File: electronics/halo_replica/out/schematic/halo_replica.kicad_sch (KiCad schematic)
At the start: 57 parts, among them J1 U.FL / IPEX MHF RECEPTACLE, U1 nRF52832-CIAA (WLCSP-50) - DR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, U2 APPLE U1 UWB SiP - DNP / UNPO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, U3 GD25LQ32C 32Mb 1.8V SPI NOR (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, U4 3-AXIS ACCELEROMETER - PART C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, U5 MAX98357A-CLASS CLASS-D AMP (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, U6 TPS62746-CLASS BUCK 3V->1V8 (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, U7 TLV9001-CLASS OP-AMP - ROLE I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, U8 FPF2487-CLASS LOAD SWITCH (LO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, U9 CANNOT DETERMINE - marking 1A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, X1 32 MHz? marking T320 / RBEV -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, X2 32.768 kHz? marking A048L - P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

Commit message: E07 synthesis: three kinds of adjacent, and the pipeline exit code as a sixth
Refinement from the comparison lane: the five cases differ in WHAT the adjacent
property was - three adjacent STATISTICS (increment permutation, off-peak noise,
area alone), one adjacent COORDINATE (between-in-x), one adjacent PATH (a guard
resolving against the search root). The path case is the one people least expect
because it is not a modelling error at all - a plumbing error wearing a control's
clothes, which no amount of thinking about the physics would have found.

Plus a sixth of the same shape from the same day: reading 'cmd | tail's exit
status instead of the command's. PIPESTATUS[0] gives the real one. The exit code
you read was adjacent to the exit code you wanted.

Co-Authored-By: Claude Opus 5 (1M context) <noreply@anthropic.com>
Claude-Session: https://claude.ai/code/session_01JRY3feHovaK2VS3mL7infx
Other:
- note added: "halo REPLICA - Apple AirTag A2187 (FCC ID BCGA2187), reconstructed. NOBODY HAS TRACED APPLE'S COPPER. Not one net here was read off a board. Every net carries a basis - MEASURED, INFERRED or CHOSEN - and NETS.md beside this file lists all of them. ONLY SEVEN OF 51 NETS ARE MEASURED: the three battery contacts and the four SWD pads O'Flynn published. The other 44 are 21 INFERRED and 23 CHOSEN."
- note removed: "halo REPLICA - Apple AirTag A2187 (FCC ID BCGA2187), reconstructed. NOBODY HAS TRACED APPLE'S COPPER. Not one net here was read off a board. Every net carries a basis - MEASURED, INFERRED or CHOSEN - and NETS.md beside this file lists all of them. Only five nets are MEASURED, and they are the SWD pads."
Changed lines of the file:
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@@
 		)
 	)
-	(text "halo REPLICA - Apple AirTag A2187 (FCC ID BCGA2187), reconstructed. NOBODY HAS TRACED APPLE'S COPPER. Not one net here was read off a board. Every net carries a basis - MEASURED, INFERRED or CHOSEN - and NETS.md beside this file lists all of them. Only five nets are MEASURED, and they are the SWD pads."
+	(text "halo REPLICA - Apple AirTag A2187 (FCC ID BCGA2187), reconstructed. NOBODY HAS TRACED APPLE'S COPPER. Not one net here was read off a board. Every net carries a basis - MEASURED, INFERRED or CHOSEN - and NETS.md beside this file lists all of them. ONLY SEVEN OF 51 NETS ARE MEASURED: the three battery contacts and the four SWD pads O'Flynn published. The other 44 are 21 INFERRED and 23 CHOSEN."
 		(exclude_from_sim no)
 		(at 12.7 388.62 0)

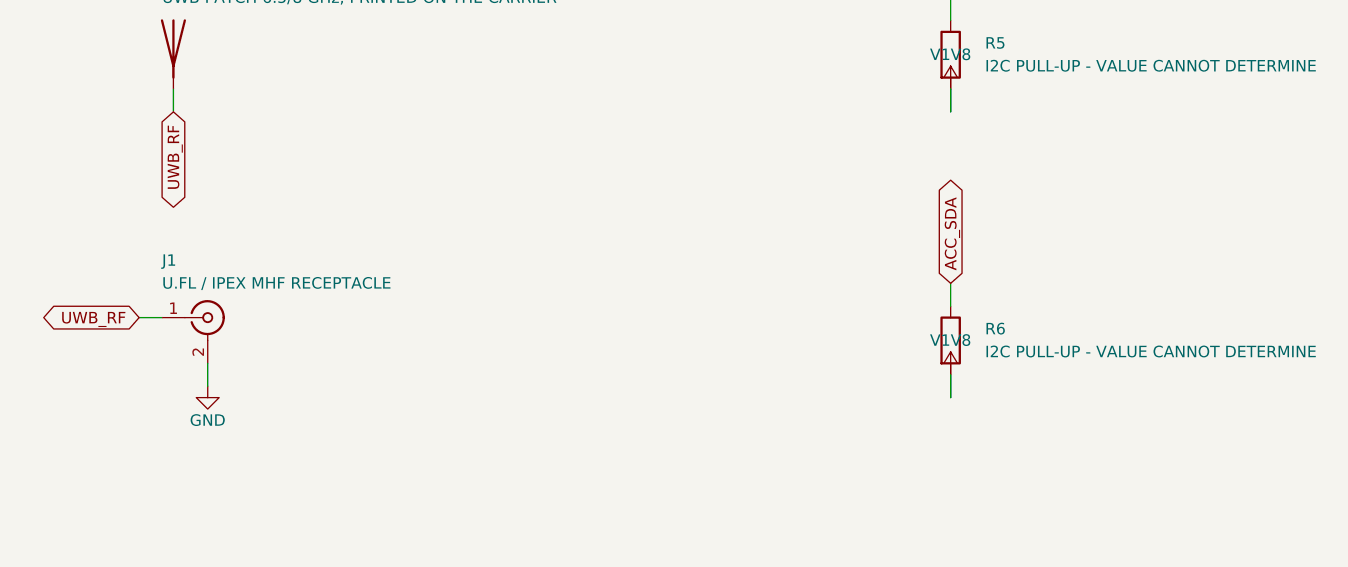
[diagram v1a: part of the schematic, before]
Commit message: L9: three legs - EXISTS, CURRENT, VALID. Existence is adjacent to currency, currency to validity
halo-cb refused to give us a clean test case and that refusal produced the third leg. It
is deliberately NOT regenerating rev_a's gerbers because the board still has 28
unconnected nets: a set cut now would be FRESH AND UNBUILDABLE, and would pass existence
AND freshness simultaneously. That is a worse artifact than a stale one precisely because
both other assertions wave it through.

  EXISTS   a file of the right kind is here and the tool can open it
  CURRENT  it is newer than every one of its sources
  VALID    its source PASSED ITS OWN CHECKS at the time it was cut

Not belt-and-braces: three genuinely different properties one artifact can independently
fail, each satisfied by something NEXT TO what we actually want.

RUN AGAINST BOTH BOARDS. rev_a: 8 of 8 exist and open - I WAS WRONG THAT IT HAD NO
GERBERS, there are twelve plus two drill files, just under out/release/board/gerber where
I had not searched. The conclusion survives for two worse reasons:
  D6 DRC     STALE by 17,616 s - it grades copper it never saw
  D7 gerbers STALE by 7,742 s AND INVALID - cut from a board with 28 unconnected nets
  D8 drill   STALE by 7,741 s AND INVALID - same
Replica: 5 of 8 exist, D2 netlist was 81 s older than its schematic when first run.

FOUR DEFECTS IN MY OWN CHECK, each found by pointing it somewhere new:
 1. The D7 glob was **/*.gbr, which catches only the DRILL MAPS. A real KiCad gerber set
    is .gtl .gbl .g1 .g2 .gts .gbs .gto .gbo .gm1 - none end in .gbr. It would have called
    a set complete while seeing none of its copper layers.
 2. The DRC probe was the bare substring "drc", which admitted drc-liveness.json and
    friends - not DRC reports at all. Now the KiCad $schema URL.
 3. read_verdict SUMMED every matching report, adding up several runs against several
    different boards and returning 1016 errors that belonged to none of them. A verdict is
    a prop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
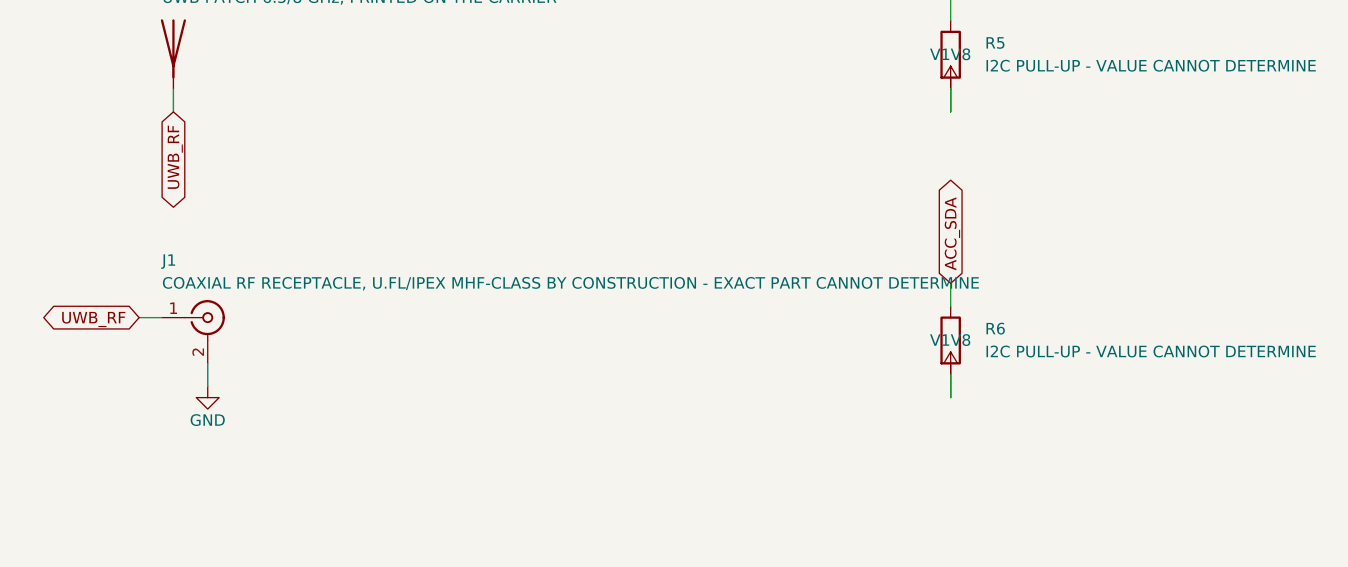
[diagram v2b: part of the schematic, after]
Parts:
- J1: value U.FL / IPEX MHF RECEPTACLE -> COAXIAL RF RECEPTACLE, U.FL/IPEX MHF-CLASS BY CONSTRUCTION - EXACT PART CANNOT DETERMINE
- X1: BOM confidence HIGH that the marking is T320 / RBEV. CANNOT DETERMINE for the manufacturer, the part number, the load capacitance and the tolerance. MEDIUM for 'this is the 32 MHz one' — that is -> HIGH that the marking is T320 / RBEV. CANNOT DETERMINE for the manufacturer, the part number, the load capacitance and the tolerance. MEDIUM for 'this is the 32 MHz one' — Catley's
- X2: BOM confidence HIGH for the marking. CANNOT DETERMINE for the part. MEDIUM for the frequency assignment, untested. -> HIGH for the marking. CANNOT DETERMINE for the part. MEDIUM for the frequency assignment, now TESTED by package geometry and SUPPORTED (see X1_vs_X2_TEST). Its aspect 1.554 and 161
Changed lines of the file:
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@@
 			)
 		)
-		(property "BOM confidence" "HIGH that the marking is T320 / RBEV. CANNOT DETERMINE for the manufacturer, the part number, the load capacitance and the tolerance. MEDIUM for 'this is the 32 MHz one' — that is "
+		(property "BOM confidence" "HIGH that the marking is T320 / RBEV. CANNOT DETERMINE for the manufacturer, the part number, the load capacitance and the tolerance. MEDIUM for 'this is the 32 MHz one' — Catley's"
 			(at 300.99 36.83 0)
 			(effects
@@
 			)
 		)
-		(property "BOM confidence" "HIGH for the marking. CANNOT DETERMINE for the part. MEDIUM for the frequency assignment, untested."
+		(property "BOM confidence" "HIGH for the marking. CANNOT DETERMINE for the part. MEDIUM for the frequency assignment, now TESTED by package geometry and SUPPORTED (see X1_vs_X2_TEST). Its aspect 1.554 and 161"
 			(at 300.99 64.77 0)
 			(effects
@@
 			)
 		)
-		(property "Value" "U.FL / IPEX MHF RECEPTACLE"
+		(property "Value" "COAXIAL RF RECEPTACLE, U.FL/IPEX MHF-CLASS BY CONSTRUCTION - EXACT PART CANNOT DETERMINE"
 			(at 441.96 96.52 0)
 			(effects

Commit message: L9: the fifth state - whose fault a clearance violation is, with the guard that stops it being a string
Three classes, and the excusing ones must PROVE it:
  DRAWN-WRONG          no pointer, BLOCKS. Our defect, and THE DEFAULT.
  MEASUREMENT-LIMITED  pointer required, BLOCKS. Not our defect and still not fabricable
                       - you cannot cut a board where two pads overlap whatever the
                       reason. It names a different fix: a measurement that can separate
                       them, not a nudged pad.
  GENUINELY-TOUCHING   pointer required, does NOT block. Same net or same feature, so
                       there is no clearance to violate.

THE DEFAULT IS THE WHOLE INCENTIVE. An unclassified violation falls back to DRAWN-WRONG,
so SILENCE MEANS OUR FAULT, NEVER APPLE'S. A lane that wants a violation excused must
produce evidence; a lane that produces nothing gets the blame.

AND THE GUARD IS THE POINT, because I raised this failure mode against the basis counter
an hour ago and it applies to my own gate: IF A VIOLATION CAN LEAVE DRAWN-WRONG BY
EDITING A STRING, THE GATE IS SOMETHING A LANE IMPROVES BY TYPING. So an excusing class
names evidence this check RESOLVES and then checks that it SUPPORTS THE CLAIM.

6 breaks, and C-4 is the one that matters:
  C-1  no classification file            -> all DRAWN-WRONG
  C-2  gap 0.0500 mm, pointer resolves   -> MEASUREMENT-LIMITED accepted
  C-3  same claim, pointer does not resolve        -> refused
  C-3b pointer resolves, names a row NOT in it     -> refused
  C-4  POINTER RESOLVES, gap 0.0900 mm is OUTSIDE the 0.0606 floor -> REFUSED
  C-5  GENUINELY-TOUCHING accepted and does not block
RESOLVING IS NOT SUPPORTING. Without C-4 the excuse is a string with a filename attached.

THE FLOOR IS DERIVED AND SAYS SO: 0.0606 mm = two genuine pixels at 33 px/mm, one edge-
location pixel on each of the two facing edges. NOT the registration hold-out of
0.1256 mm, which would excuse roughly twice as m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
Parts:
- added TP19: SPI_MOSI (O'Flynn TP19), TestPoint:TestPoint_Pad_D1.0mm, symbol Connector:TestPoint
- added TP20: SPI_MISO (O'Flynn TP20), TestPoint:TestPoint_Pad_D1.0mm, symbol Connector:TestPoint
- added TP21: V1V8_SW (O'Flynn TP21), TestPoint:TestPoint_Pad_D1.0mm, symbol Connector:TestPoint
- added TP22: SPI_SCK (O'Flynn TP22), TestPoint:TestPoint_Pad_D1.0mm, symbol Connector:TestPoint
- added TP24: FLASH_nCS (O'Flynn TP24), TestPoint:TestPoint_Pad_D1.0mm, symbol Connector:TestPoint
- added TP29: GND (O'Flynn TP29), TestPoint:TestPoint_Pad_D1.0mm, symbol Connector:TestPoint
- added TP34: V1V8 (O'Flynn TP34), TestPoint:TestPoint_Pad_D1.0mm, symbol Connector:TestPoint
- added TP5: VBAT_SNS_P2 (O'Flynn TP5), TestPoint:TestPoint_Pad_D1.0mm, symbol Connector:TestPoint
- added TP6: VBAT_RAW (O'Flynn TP6), TestPoint:TestPoint_Pad_D1.0mm, symbol Connector:TestPoint
- added TP7: GND (O'Flynn TP7), TestPoint:TestPoint_Pad_D1.0mm, symbol Connector:TestPoint
- added TP9: P0.26 - FUNCTION CANNOT DETERMINE, TestPoint:TestPoint_Pad_D1.0mm, symbol Connector:TestPoint
- TP30: Note O'Flynn's TP30 = nRST. On nRF52832 that is P0.21/nRESET. TH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 -> O'Flynn's table, verbatim: '30 | nRF ball H1 (P0.21/nRST)'.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; Source research/fetched/A-oflynn-testpoints-and-glitch-repos.md -> research/fetched/A-oflynn-testpoints-and-glitch-repos.md — 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
- TP31: Note O'Flynn's TP31 = SWO, P0.18 on this die. THESE FOUR ARE THE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 -> O'Flynn's table, verbatim: '31 | nRF ball H2 (P0.18/SWO)'. 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; Source research/fetched/A-oflynn-testpoints-and-glitch-repos.md -> research/fetched/A-oflynn-testpoints-and-glitch-repos.md — 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
- TP35: Note O'Flynn's TP35 = SWCLK. THESE FOUR ARE THE ONLY NETS ON THI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 -> O'Flynn's table, verbatim: '35 | nRF ball F1 (SWCLK)'. No G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; Source research/fetched/A-oflynn-testpoints-and-glitch-repos.md -> research/fetched/A-oflynn-testpoints-and-glitch-repos.md — 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
- TP36: Note O'Flynn's TP36 = SWDIO. THESE FOUR ARE THE ONLY NETS ON THI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 -> O'Flynn's table, verbatim: '36 | nRF ball G1 (SWDIO)'. THES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; Source research/fetched/A-oflynn-testpoints-and-glitch-repos.md -> research/fetched/A-oflynn-testpoints-and-glitch-repos.md — 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
- U1: Note THE PART IS CERTAIN AND THE PACKAGE IS SUBSTITUTED. Marking 'N52832 CIAAE0 2102JK' was read off the die photograph by lane L3 - fully legible, three lines. CIAA is WLCSP-50 and NO SOURCED BALL MAP EXISTS IN THIS REPOSITORY, so this sheet uses the QFN-48 (QFAA) symbol of the SAME DIE. The netlist is right by signal name; the pin NUMBERS are QFAA's. Inventing 50 ball designators is what DECISIONS.md D9 forbids. -> THE PART IS CERTAIN AND THE PACKAGE IS SUBSTITUTED. Marking 'N52832 CIAAE0 2102JK' was read off the die photograph by lane L3 - fully legible, three lines. CIAA is WLCSP-50 and NO COMPLETE BALL MAP IS SOURCED HERE - O'Flynn's table gives TEN of the fifty (D3, E2, F1, F4, G1, G3, H1, H2, H3, H4) - so this sheet uses the QFN-48 (QFAA) symbol of the SAME DIE. The netlist is right by signal name; the pin NUMBERS are QFAA's. Inventing 50 ball designators is what DECISIONS.md D9 forbids.
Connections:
- net EN_PERIPH: now also U1.15 (P0.12); no longer U1.18 (P0.15)
- net FLASH_nCS: now also TP24.1
- net GND: now also TP29.1, TP7.1
- net I2S_BCLK: now also U1.16 (P0.13); no longer U1.19 (P0.16)
- net I2S_LRCLK: now also U1.17 (P0.14); no longer U1.20 (P0.17)
- net SPI_MISO: now also U1.18 (P0.15), TP20.1; no longer U1.17 (P0.14)
- net SPI_MOSI: now also U1.19 (P0.16), TP19.1; no longer U1.16 (P0.13)
- net SPI_SCK: now also U1.20 (P0.17), TP22.1; no longer U1.15 (P0.12)
- net V1V8: now also TP34.1
- net V1V8_SW: now also TP21.1
- net VBAT_RAW: now also TP6.1
- net VBAT_SNS_P2: now also TP5.1
- net TP9_P0.26: now reaches U1.38 (P0.26)
- net TP9_P0.26: now also TP9.1
- no-connect marks 14 -> 13
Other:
- note added: "A CONTRADICTION INSIDE O'FLYNN'S OWN TABLE, CARRIED NOT RESOLVED: row 8 reads 'nRF ball E2 (P0.16)' and row 19 reads 'nRF ball H3 (P0.16)'. Two different balls with one GPIO number; one is a transcription error. This sheet takes row 19 because the SPI block's four balls H3/H4/G3/F4 are a coherent group, and TP8 IS DELIBERATELY ABSENT rather than drawn on a guess."
- note added: "FOUR NETS ON THIS SHEET WERE WRONG UNTIL A CHECK FORCED SOMEBODY TO OPEN THE FILE THEY ALREADY CITED. The flash bus was drawn on P0.12/P0.13/P0.14 as a free CHOICE. O'Flynn's test-point table gives it by pad, by nRF BALL and by GPIO: SCLK on P0.17 (ball G3), COPI on P0.16 (H3), CIPO on P0.15 (H4), CS on P0.11 (F4). Three of the four were wrong and the fourth was right by luck. The bus is MEASURED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"
- note added: "TEN CIAA BALLS ARE SOURCED, AND FORTY ARE NOT. O'Flynn's table names nRF ball designators for D3, E2, F1, F4, G1, G3, H1, H2, H3 and H4. That is not a ball map and does not make one - the package here is still the QFN-48 substitution - but it is ten more than this sheet first claimed existed, and L12 should have them when it draws the WLCSP land."
- note added: "THE PACKAGES ARE NOT APPLE'S PACKAGES. U1 is an nRF52832-CIAA, WLCSP-50, drawn with the QFN-48 (QFAA) symbol of the same die because no COMPLETE CIAA ball map is sourced here (ten balls are; forty are not). U3 is a WLCSP-10 drawn as WSON-8. U5 is a WLCSP drawn as TQFP-16. THE NETLIST IS RIGHT BY SIGNAL NAME AND THE PIN NUMBERS ARE NOT APPLE'S. Every part carries an FP-basis field; L12 owns the la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"
- note added: "THE iFIXIT ARGUMENT IS NOW SETTLED BY MEASUREMENT, not by self-consistency. O'Flynn, verbatim: 'The nrf controls power to the SPI flash, so you need to override it by supplying 1.8V on test point 21', and 'most of time the flash is powered off and thus the pins are tri-stated'. The flash sits on a switched 1.8 V rail the MCU commands - which is what this sheet drew from the argument that a load s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"
- note added: "halo REPLICA - Apple AirTag A2187 (FCC ID BCGA2187), reconstructed. NOBODY HAS TRACED APPLE'S COPPER. Every net carries a basis - MEASURED, INFERRED or CHOSEN - and NETS.md beside this file lists all of them with the counts DERIVED, never typed. 13 of 52 nets are MEASURED, and every one of those names a FILE AND A STRING THAT MUST BE IN IT, checked at build time. The other 39 are inference and ch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"
- note removed: "THE PACKAGES ARE NOT APPLE'S PACKAGES. U1 is an nRF52832-CIAA, WLCSP-50, drawn with the QFN-48 (QFAA) symbol of the same die because no CIAA ball map is sourced in this repository. U3 is a WLCSP-10 drawn as WSON-8. U5 is a WLCSP drawn as TQFP-16. THE NETLIST IS RIGHT BY SIGNAL NAME AND THE PIN NUMBERS ARE NOT APPLE'S. Every part carries an FP-basis field; L12 owns the land patterns."
- note removed: "halo REPLICA - Apple AirTag A2187 (FCC ID BCGA2187), reconstructed. NOBODY HAS TRACED APPLE'S COPPER. Not one net here was read off a board. Every net carries a basis - MEASURED, INFERRED or CHOSEN - and NETS.md beside this file lists all of them. ONLY SEVEN OF 51 NETS ARE MEASURED: the three battery contacts and the four SWD pads O'Flynn published. The other 44 are 21 INFERRED and 23 CHOSEN."
